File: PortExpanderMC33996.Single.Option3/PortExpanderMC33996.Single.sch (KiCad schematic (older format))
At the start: 8 parts, among them J1 DEBUG_CON_01X09, J2 VIKING_CON_01X09, J3 VIKING_CON_01X09, J4 SATA_CON_14P, U1 MC33996EKR2

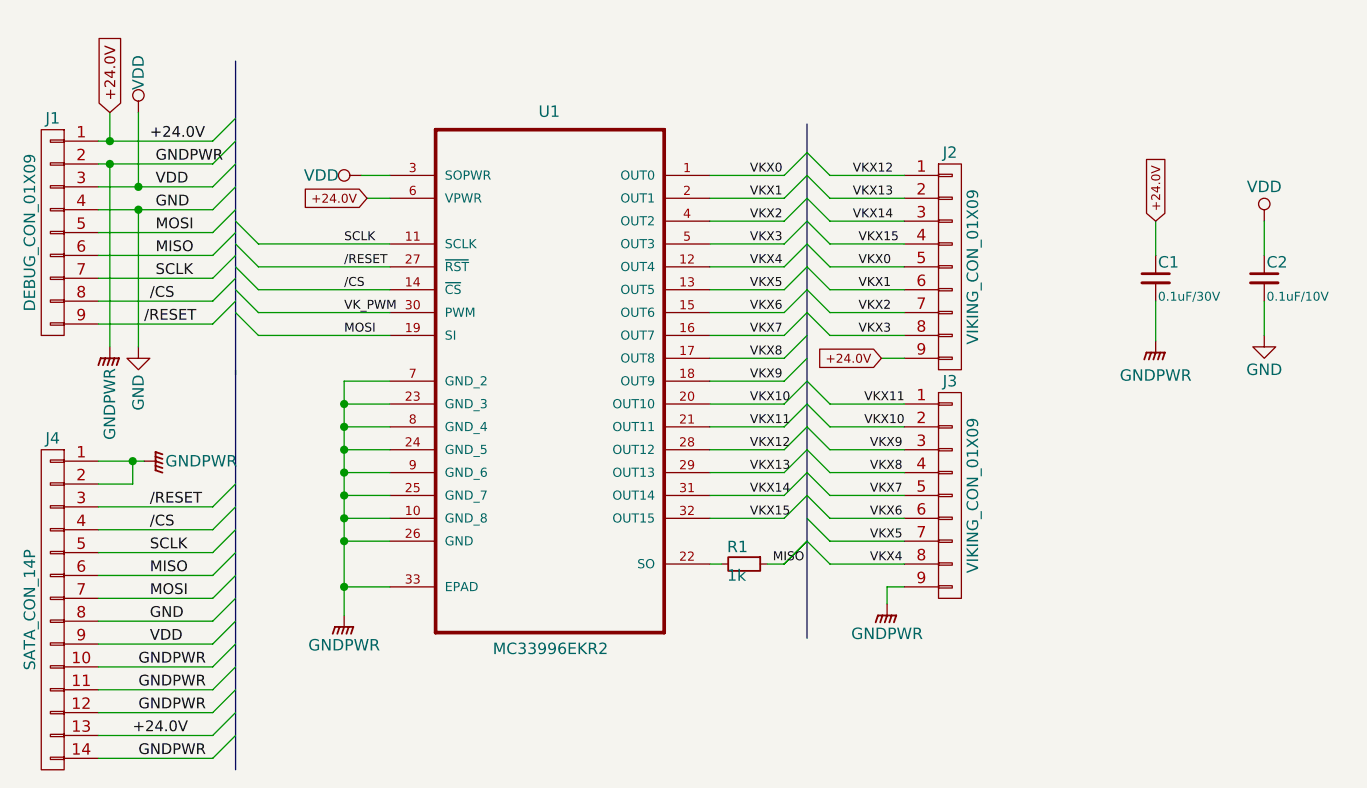
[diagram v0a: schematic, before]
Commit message: Revision de PCbs + generacion de nuevos archivos Gerber
  - Se corrigen pads de pin headers
  - Se revisan
  - MainBoard option 2
  - PortExpander MC33996.Option3
  - GpibPortExpanderPCA6408A.Option3
  - Se generan Gerber + Vistas 3D
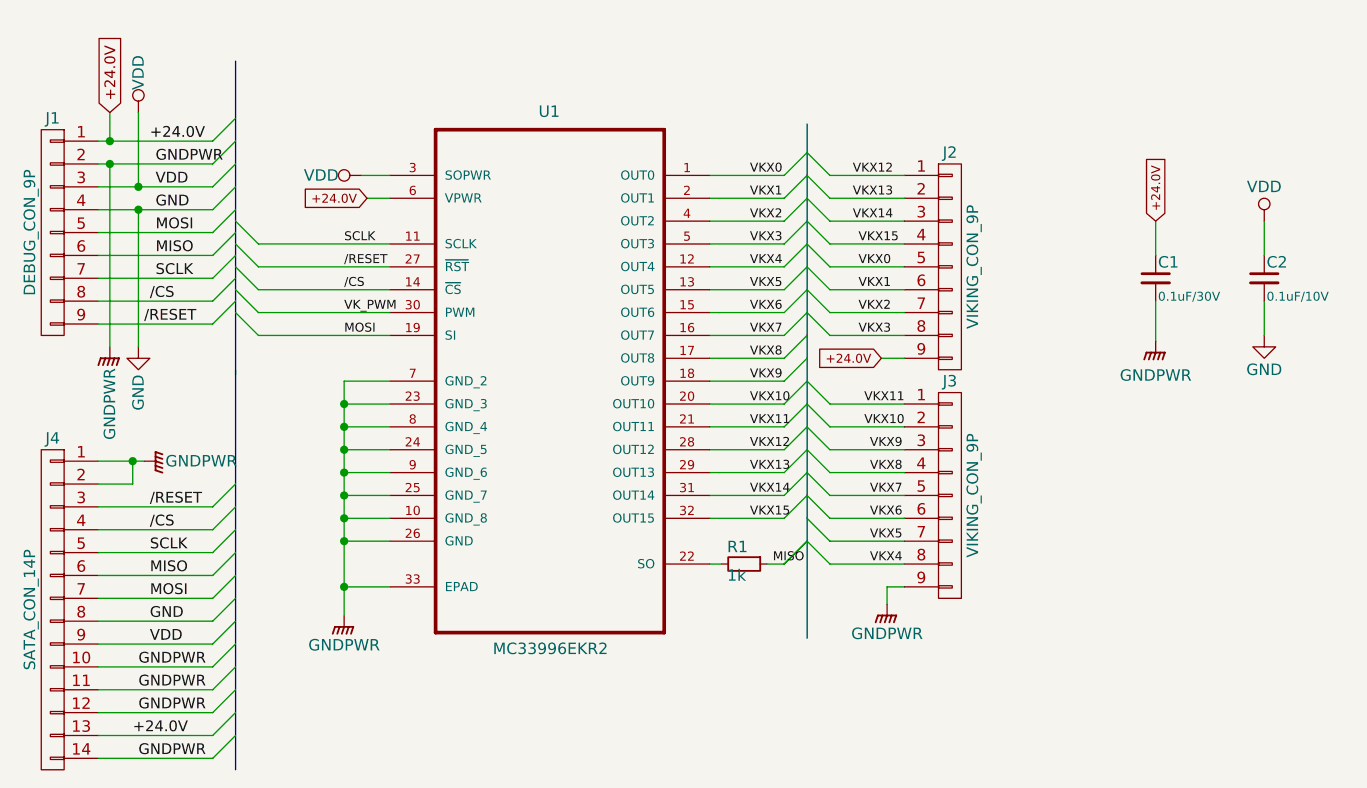
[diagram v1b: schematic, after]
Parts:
- J1: value DEBUG_CON_01X09 -> DEBUG_CON_9P; footprint Pin_Headers:Pin_Header_Straight_1x09_Pitch2.54mm -> CenditFootprints:DEBUG_CON_9P
- J2, J3: value VIKING_CON_01X09 -> VIKING_CON_9P; footprint Pin_Headers:Pin_Header_Straight_1x09_Pitch2.54mm -> CenditFootprints:VIKING_HEADER_9P
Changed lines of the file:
@@
 LIBS:74xx
 LIBS:cmos4000
+LIBS:eSim_Analog
+LIBS:eSim_Devices
+LIBS:eSim_Digital
+LIBS:eSim_Hybrid
+LIBS:eSim_Miscellaneous
+LIBS:eSim_Power
+LIBS:eSim_Sources
+LIBS:eSim_Subckt
+LIBS:eSim_User
+LIBS:eSim_Plot
+LIBS:eSim_PSpice
 LIBS:PortExpanderMC33996.Single-cache
 EELAYER 25 0
@@
 P 7525 3175
 F 0 "J2" H 7525 3675 50  0000 C CNN
-F 1 "VIKING_CON_01X09" V 7625 3175 50  0000 C CNN
-F 2 "Pin_Headers:Pin_Header_Straight_1x09_Pitch2.54mm" H 7525 3175 50  0001 C CNN
+F 1 "VIKING_CON_9P" V 7625 3175 50  0000 C CNN
+F 2 "CenditFootprints:VIKING_HEADER_9P" H 7525 3175 50  0001 C CNN
 F 3 "" H 7525 3175 50  0001 C CNN
 	1    7525 3175
@@
 P 7525 4175
 F 0 "J3" H 7525 4675 50  0000 C CNN
-F 1 "VIKING_CON_01X09" V 7625 4175 50  0000 C CNN
-F 2 "Pin_Headers:Pin_Header_Straight_1x09_Pitch2.54mm" H 7525 4175 50  0001 C CNN
+F 1 "VIKING_CON_9P" V 7625 4175 50  0000 C CNN
+F 2 "CenditFootprints:VIKING_HEADER_9P" H 7525 4175 50  0001 C CNN
 F 3 "" H 7525 4175 50  0001 C CNN
 	1    7525 4175
@@
 P 3600 3025
 F 0 "J1" H 3600 3525 50  0000 C CNN
-F 1 "DEBUG_CON_01X09" V 3700 3025 50  0000 C CNN
-F 2 "Pin_Headers:Pin_Header_Straight_1x09_Pitch2.54mm" H 3600 3025 50  0001 C CNN
+F 1 "DEBUG_CON_9P" V 3700 3025 50  0000 C CNN
+F 2 "CenditFootprints:DEBUG_CON_9P" H 3600 3025 50  0001 C CNN
 F 3 "" H 3600 3025 50  0001 C CNN
 	1    3600 3025
@@
 Connection ~ 3950 4025
 $Comp
-L GNDPWR #PWR?
+L GNDPWR #PWR010
 U 1 1 5A542FC3
 P 4000 4025
-F 0 "#PWR?" H 4000 3825 50  0001 C CNN
+F 0 "#PWR010" H 4000 3825 50  0001 C CNN
 F 1 "GNDPWR" V 4000 3775 50  0000 C CNN
 F 2 "" H 4000 3975 50  0000 C CNN
